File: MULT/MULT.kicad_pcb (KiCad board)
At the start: 2 copper layers, 50 x 22.5 mm, 8 parts, among them J1 AudioJack2_SwitchT, J2 AudioJack2_SwitchT, J3 AudioJack2_SwitchT, J4 AudioJack2_SwitchT, J5 AudioJack2_SwitchT, J6 AudioJack2_SwitchT, J7 AudioJack2_SwitchT, J8 AudioJack2_SwitchT

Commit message: Add MULT front panel
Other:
- board text added: "Passive MULT"
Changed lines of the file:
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@@
 		)
 		(property "Value" "AudioJack2_SwitchT"
-			(at 0 -8.25 360)
+			(at 0 -8.25 0)
 			(layer "F.Fab")
 			(effects
@@
 		)
 		(property "Footprint" "Custom_FP:PJ398SM"
-			(at 0 0 360)
+			(at 0 0 0)
 			(layer "F.Fab")
 			(hide yes)
@@
 		)
 		(property "Datasheet" ""
-			(at 0 0 360)
+			(at 0 0 0)
 			(layer "F.Fab")
 			(hide yes)
@@
 		)
 		(property "Description" ""
-			(at 0 0 360)
+			(at 0 0 0)
 			(layer "F.Fab")
 			(hide yes)
@@
 		)
 		(property "Value" "AudioJack2_SwitchT"
-			(at 0 -8.25 360)
+			(at 0 -8.25 0)
 			(layer "F.Fab")
 			(effects
@@
 		)
 		(property "Footprint" "Custom_FP:PJ398SM"
-			(at 0 0 360)
+			(at 0 0 0)
 			(layer "F.Fab")
 			(hide yes)
@@
 		)
 		(property "Datasheet" ""
-			(at 0 0 360)
+			(at 0 0 0)
 			(layer "F.Fab")
 			(hide yes)
@@
 		)
 		(property "Description" ""
-			(at 0 0 360)
+			(at 0 0 0)
 			(layer "F.Fab")
 			(hide yes)
@@
 		)
 		(property "Value" "AudioJack2_SwitchT"
-			(at 0 -8.25 360)
+			(at 0 -8.25 0)
 			(layer "F.Fab")
 			(effects
@@
 		)
 		(property "Footprint" "Custom_FP:PJ398SM"
-			(at 0 0 360)
+			(at 0 0 0)
 			(layer "F.Fab")
 			(hide yes)
@@
 		)
 		(property "Datasheet" ""
-			(at 0 0 360)
+			(at 0 0 0)
 			(layer "F.Fab")
 			(hide yes)
@@
 		)
 		(property "Description" ""
-			(at 0 0 360)
+			(at 0 0 0)
 			(layer "F.Fab")
 			(hide yes)
@@
 		)
 		(property "Value" "AudioJack2_SwitchT"
-			(at 0 -8.25 360)
+			(at 0 -8.25 0)
 			(layer "F.Fab")
 			(effects
@@
 		)
 		(property "Footprint" "Custom_FP:PJ398SM"
-			(at 0 0 360)
+			(at 0 0 0)
 			(layer "F.Fab")
 			(hide yes)
@@
 		)
 		(property "Datasheet" ""
-			(at 0 0 360)
+			(at 0 0 0)
 			(layer "F.Fab")
 			(hide yes)
@@
 		)
 		(property "Description" ""
-			(at 0 0 360)
+			(at 0 0 0)
 			(layer "F.Fab")
 			(hide yes)
@@
 		)
 		(property "Value" "AudioJack2_SwitchT"
-			(at 0 -8.25 360)
+			(at 0 -8.25 0)
 			(layer "F.Fab")
 			(effects
@@
 		)
 		(property "Footprint" "Custom_FP:PJ398SM"
-			(at 0 0 360)
+			(at 0 0 0)
 			(layer "F.Fab")
 			(hide yes)
@@
 		)
 		(property "Datasheet" ""
-			(at 0 0 360)
+			(at 0 0 0)
 			(layer "F.Fab")
 			(hide yes)
@@
 		)
 		(property "Description" ""
-			(at 0 0 360)
+			(at 0 0 0)
 			(layer "F.Fab")
 			(hide yes)
@@
 		(layer "Edge.Cuts")
 	)
+	(gr_text "Passive\nMULT"
+		(at 112.1 118.25 0)
+		(layer "B.SilkS")
+		(effects
+			(font
+				(size 1 1)
+				(thickness 0.15)
+			)
+			(justify left bottom mirror)
+		)
+	)
 	(segment

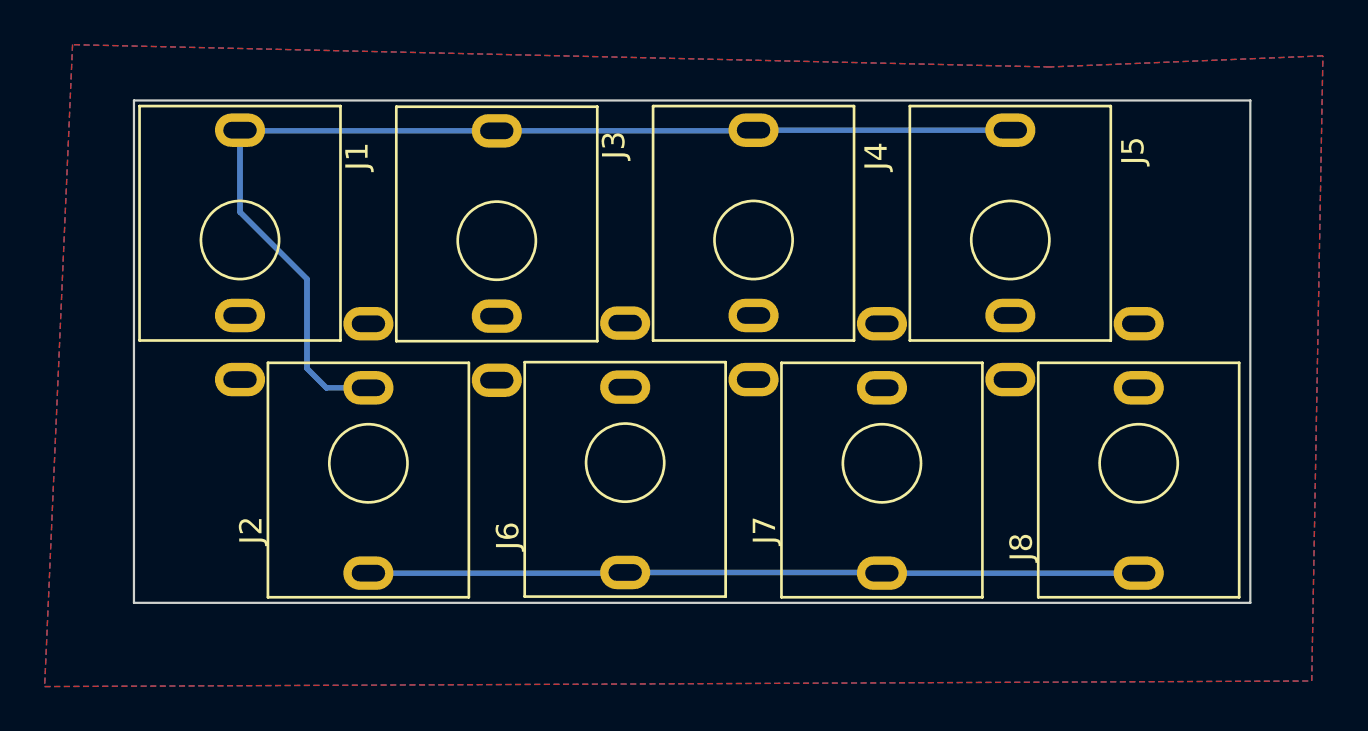
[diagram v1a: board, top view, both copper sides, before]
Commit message: Create MULT front panel
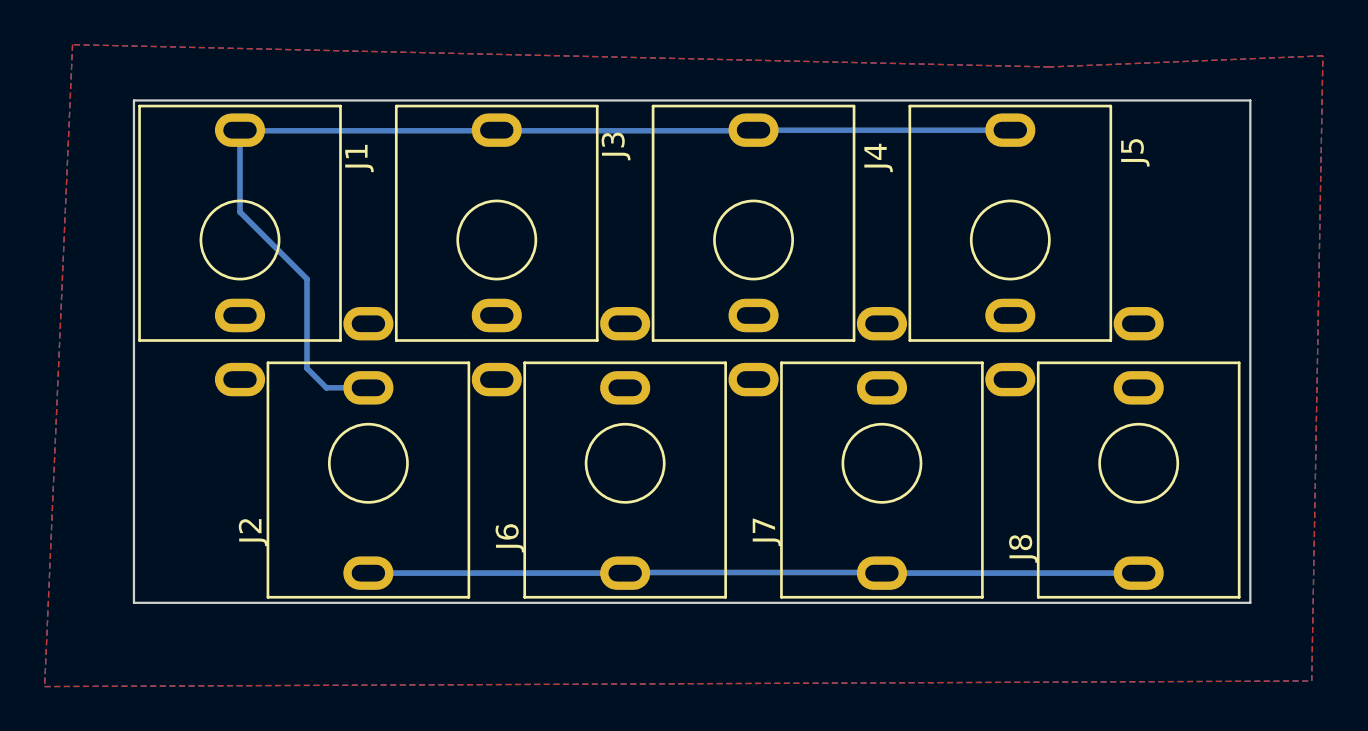
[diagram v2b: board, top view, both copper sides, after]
